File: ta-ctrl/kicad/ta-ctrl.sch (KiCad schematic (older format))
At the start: 24 parts, among them J1 PinSocket_16_ctrl, J2 PinSocket_16_ctrl, J3 MountingHole_ctrl, J4 PinSocket_4_ctrl, J5 PinSocket_4_ctrl, J6 PinSocket_5_ctrl, J7 PinSocket_5_ctrl, U1 LSF0204, U2 LSF0204, U3 LSF0204

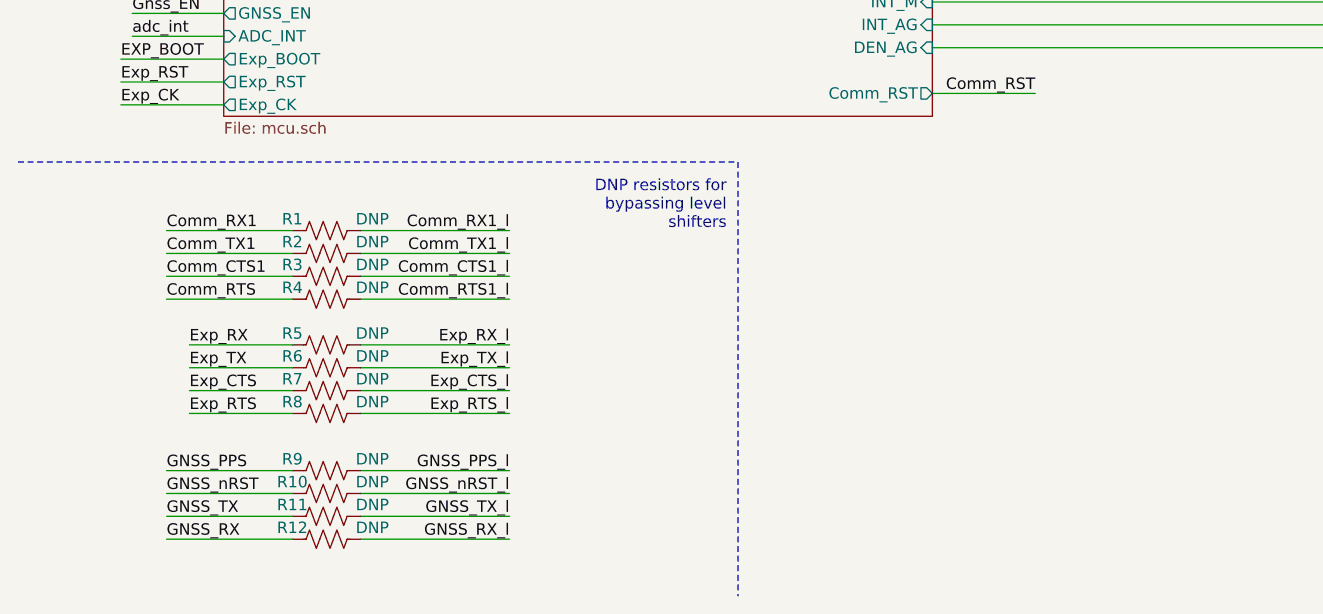
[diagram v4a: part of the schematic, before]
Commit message: updated and checked all footprints, added a diode too
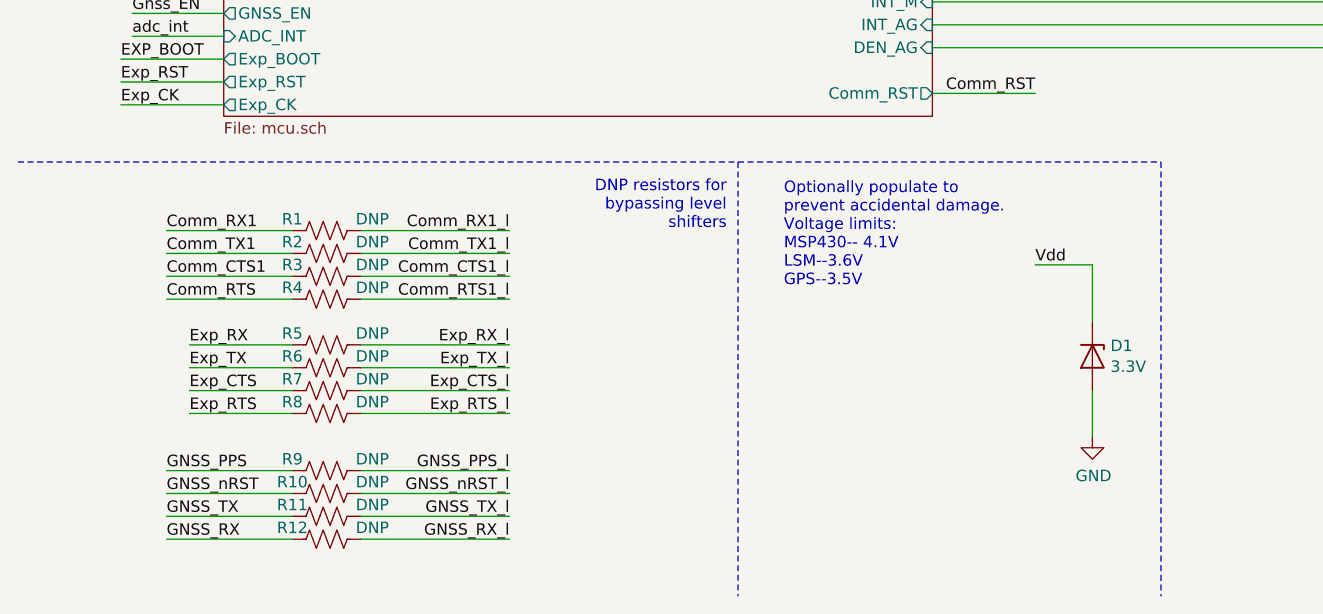
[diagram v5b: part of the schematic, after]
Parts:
- added D1: 3.3V, ta-ctrl:D_SOD-323F, symbol Device:D_Zener
- J1, J2: footprint (none) -> ta-ctrl:PinSocket_1x16_TartanArtibeus_ctrl_cpy
- J3: footprint (none) -> ta-ctrl:MountingHoles_TartanArtibeus_ctrl_cpy
- J4, J5: footprint (none) -> ta-ctrl:PinSocket_1x4_TartanArtibeus_ctrl_cpy
- R1, R10, R11, R12, R13, R14, R2, R3, R4, R5, R6, R7, R8, R9: footprint (none) -> ta-ctrl:R_0603_1608Metric_ctrl_cpy
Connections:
- net GND: now also D1.2 (A)
- net Vdd: now also D1.1 (K)
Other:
- note added: "Optionally populate to\nprevent accidental damage.\nVoltage limits:\nMSP430-- 4.1V\nLSM--3.6V\nGPS--3.5V\n"
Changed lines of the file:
@@
 F 0 "J1" H 1575 1165 50  0000 C CNN
 F 1 "PinSocket_16_ctrl" H 1575 1074 50  0000 C CNN
-F 2 "" H 1150 850 50  0001 C CNN
+F 2 "ta-ctrl:PinSocket_1x16_TartanArtibeus_ctrl_cpy" H 1150 850 50  0001 C CNN
 F 3 "" H 1150 850 50  0001 C CNN
 	1    1550 850
@@
 F 0 "J4" H 3828 963 50  0000 L CNN
 F 1 "PinSocket_4_ctrl" H 3828 872 50  0000 L CNN
-F 2 "" H 3500 850 50  0001 C CNN
+F 2 "ta-ctrl:PinSocket_1x4_TartanArtibeus_ctrl_cpy" H 3500 850 50  0001 C CNN
 F 3 "" H 3500 850 50  0001 C CNN
 	1    3550 850
@@
 F 0 "J5" H 3828 1713 50  0000 L CNN
 F 1 "PinSocket_4_ctrl" H 3828 1622 50  0000 L CNN
-F 2 "" H 3500 1600 50  0001 C CNN
+F 2 "ta-ctrl:PinSocket_1x4_TartanArtibeus_ctrl_cpy" H 3500 1600 50  0001 C CNN
 F 3 "" H 3500 1600 50  0001 C CNN
 	1    3550 1600
@@
 F 0 "J3" H 3728 2563 50  0000 L CNN
 F 1 "MountingHole_ctrl" H 3728 2472 50  0000 L CNN
-F 2 "" H 3300 2450 50  0001 C CNN
+F 2 "ta-ctrl:MountingHoles_TartanArtibeus_ctrl_cpy" H 3300 2450 50  0001 C CNN
 F 3 "" H 3300 2450 50  0001 C CNN
 	1    3450 2450
@@
 F 0 "J2" H 1575 2415 50  0000 C CNN
 F 1 "PinSocket_16_ctrl" H 1575 2324 50  0000 C CNN
-F 2 "" H 1150 2100 50  0001 C CNN
+F 2 "ta-ctrl:PinSocket_1x16_TartanArtibeus_ctrl_cpy" H 1150 2100 50  0001 C CNN
 F 3 "" H 1150 2100 50  0001 C CNN
 	1    1550 2100
@@
 F 1 "LSF0204" H 7050 1734 50  0000 C CNN
 F 2 "ta-ctrl:TSSOP-14" H 6850 1200 50  0001 C CNN
-F 3 "" H 6850 1200 50  0001 C CNN
+F 3 "https://www.ti.com/lit/ds/symlink/lsf0204-q1.pdf?HQS=TI-null-null-digikeymode-df-pf-null-wwe&ts=1595462922658" H 6850 1200 50  0001 C CNN
 	1    7050 1200
 	1    0    0    -1
@@
 F 1 "LSF0204" H 9400 1784 50  0000 C CNN
 F 2 "ta-ctrl:TSSOP-14" H 9200 1250 50  0001 C CNN
-F 3 "" H 9200 1250 50  0001 C CNN
+F 3 "https://www.ti.com/lit/ds/symlink/lsf0204-q1.pdf?HQS=TI-null-null-digikeymode-df-pf-null-wwe&ts=1595462922658" H 9200 1250 50  0001 C CNN
 	1    9400 1250
 	1    0    0    -1
@@
 F 1 "LSF0204" H 8100 3034 50  0000 C CNN
 F 2 "ta-ctrl:TSSOP-14" H 7900 2500 50  0001 C CNN
-F 3 "" H 7900 2500 50  0001 C CNN
+F 3 "https://www.ti.com/lit/ds/symlink/lsf0204-q1.pdf?HQS=TI-null-null-digikeymode-df-pf-null-wwe&ts=1595462922658" H 7900 2500 50  0001 C CNN
 	1    8100 2500
 	1    0    0    -1
 $EndComp
 $Comp
-L power:GND #PWR06
+L power:GND #PWR07
 U 1 1 5F1A8EDE
 P 6550 1600
-F 0 "#PWR06" H 6550 1350 50  0001 C CNN
+F 0 "#PWR07" H 6550 1350 50  0001 C CNN
 F 1 "GND" H 6555 1427 50  0000 C CNN
 F 2 "" H 6550 1600 50  0001 C CNN
@@
 	6550 1400 6550 1600
 $Comp
-L power:GND #PWR07
+L power:GND #PWR08
 U 1 1 5F1B0754
 P 7500 2900
-F 0 "#PWR07" H 7500 2650 50  0001 C CNN
+F 0 "#PWR08" H 7500 2650 50  0001 C CNN
 F 1 "GND" H 7505 2727 50  0000 C CNN
 F 2 "" H 7500 2900 50  0001 C CNN
@@
 	7500 2700 7650 2700
 $Comp
-L power:GND #PWR08
+L power:GND #PWR09
 U 1 1 5F1B8049
 P 8800 1650
-F 0 "#PWR08" H 8800 1400 50  0001 C CNN
+F 0 "#PWR09" H 8800 1400 50  0001 C CNN
 F 1 "GND" H 8805 1477 50  0000 C CNN
 F 2 "" H 8800 1650 50  0001 C CNN
@@
 F 0 "R13" H 9568 2046 50  0000 L CNN
 F 1 "10K" H 9568 1955 50  0000 L CNN
-F 2 "" V 9540 1990 50  0001 C CNN
+F 2 "ta-ctrl:R_0603_1608Metric_ctrl_cpy" V 9540 1990 50  0001 C CNN
 F 3 "~" H 9500 2000 50  0001 C CNN
 	1    9500 2000
@@
 F 0 "R14" H 9918 2046 50  0000 L CNN
 F 1 "10K" H 9918 1955 50  0000 L CNN
-F 2 "" V 9890 1990 50  0001 C CNN
+F 2 "ta-ctrl:R_0603_1608Metric_ctrl_cpy" V 9890 1990 50  0001 C CNN
 F 3 "~" H 9850 2000 50  0001 C CNN
 	1    9850 2000
@@
 F 0 "R3" V 1800 6450 50  0000 C CNN
 F 1 "DNP" V 1800 6800 50  0000 C CNN
-F 2 "" V 1890 6590 50  0001 C CNN
+F 2 "ta-ctrl:R_0603_1608Metric_ctrl_cpy" V 1890 6590 50  0001 C CNN
 F 3 "~" H 1850 6600 50  0001 C CNN
 	1    1850 6600
@@
 F 0 "R2" V 1800 6350 50  0000 C CNN
 F 1 "DNP" V 1800 6700 50  0000 C CNN
-F 2 "" V 1890 6490 50  0001 C CNN
+F 2 "ta-ctrl:R_0603_1608Metric_ctrl_cpy" V 1890 6490 50  0001 C CNN
 F 3 "~" H 1850 6500 50  0001 C CNN
 	1    1850 6500
@@
 F 0 "R1" V 1800 6250 50  0000 C CNN
 F 1 "DNP" V 1800 6600 50  0000 C CNN
-F 2 "" V 1890 6390 50  0001 C CNN
+F 2 "ta-ctrl:R_0603_1608Metric_ctrl_cpy" V 1890 6390 50  0001 C CNN
 F 3 "~" H 1850 6400 50  0001 C CNN
 	1    1850 6400
@@
 F 0 "R4" V 1800 6550 50  0000 C CNN
 F 1 "DNP" V 1800 6900 50  0000 C CNN
-F 2 "" V 1890 6690 50  0001 C CNN
+F 2 "ta-ctrl:R_0603_1608Metric_ctrl_cpy" V 1890 6690 50  0001 C CNN
 F 3 "~" H 1850 6700 50  0001 C CNN
 	1    1850 6700
@@
 F 0 "R7" V 1800 6950 50  0000 C CNN
 F 1 "DNP" V 1800 7300 50  0000 C CNN
-F 2 "" V 1890 7090 50  0001 C CNN
+F 2 "ta-ctrl:R_0603_1608Metric_ctrl_cpy" V 1890 7090 50  0001 C CNN
 F 3 "~" H 1850 7100 50  0001 C CNN
 	1    1850 7100
@@
 F 0 "R6" V 1800 6850 50  0000 C CNN
 F 1 "DNP" V 1800 7200 50  0000 C CNN
-F 2 "" V 1890 6990 50  0001 C CNN
+F 2 "ta-ctrl:R_0603_1608Metric_ctrl_cpy" V 1890 6990 50  0001 C CNN
 F 3 "~" H 1850 7000 50  0001 C CNN
 	1    1850 7000
@@
 F 0 "R5" V 1800 6750 50  0000 C CNN
 F 1 "DNP" V 1800 7100 50  0000 C CNN
-F 2 "" V 1890 6890 50  0001 C CNN
+F 2 "ta-ctrl:R_0603_1608Metric_ctrl_cpy" V 1890 6890 50  0001 C CNN
 F 3 "~" H 1850 6900 50  0001 C CNN
 	1    1850 6900
@@
 F 0 "R8" V 1800 7050 50  0000 C CNN
 F 1 "DNP" V 1800 7400 50  0000 C CNN
-F 2 "" V 1890 7190 50  0001 C CNN
+F 2 "ta-ctrl:R_0603_1608Metric_ctrl_cpy" V 1890 7190 50  0001 C CNN
 F 3 "~" H 1850 7200 50  0001 C CNN
 	1    1850 7200
@@
 F 0 "R11" V 1800 7500 50  0000 C CNN
 F 1 "DNP" V 1800 7850 50  0000 C CNN
-F 2 "" V 1890 7640 50  0001 C CNN
+F 2 "ta-ctrl:R_0603_1608Metric_ctrl_cpy" V 1890 7640 50  0001 C CNN
 F 3 "~" H 1850 7650 50  0001 C CNN
 	1    1850 7650
@@
 F 0 "R10" V 1800 7400 50  0000 C CNN
 F 1 "DNP" V 1800 7750 50  0000 C CNN
-F 2 "" V 1890 7540 50  0001 C CNN
+F 2 "ta-ctrl:R_0603_1608Metric_ctrl_cpy" V 1890 7540 50  0001 C CNN
 F 3 "~" H 1850 7550 50  0001 C CNN
 	1    1850 7550
@@
 F 0 "R9" V 1800 7300 50  0000 C CNN
 F 1 "DNP" V 1800 7650 50  0000 C CNN
-F 2 "" V 1890 7440 50  0001 C CNN
+F 2 "ta-ctrl:R_0603_1608Metric_ctrl_cpy" V 1890 7440 50  0001 C CNN
 F 3 "~" H 1850 7450 50  0001 C CNN
 	1    1850 7450
@@
 F 0 "R12" V 1800 7600 50  0000 C CNN
 F 1 "DNP" V 1800 7950 50  0000 C CNN
-F 2 "" V 1890 7740 50  0001 C CNN
+F 2 "ta-ctrl:R_0603_1608Metric_ctrl_cpy" V 1890 7740 50  0001 C CNN
 F 3 "~" H 1850 7750 50  0001 C CNN
 	1    1850 7750
@@
 Wire Wire Line
 	1150 7750 1700 7750
-Wire Notes Line
-	500  6100 3650 6100
 Wire Notes Line
 	3650 6100 3650 8000
@@
 Wire Wire Line
 	5050 2600 5050 2700
+Text Label 4950 6550 0    50   ~ 0
+Vdd
+Wire Wire Line
+	4950 6550 5200 6550
+Wire Wire Line
+	5200 6550 5200 6800
+$Comp
+L Device:D_Zener D1
+U 1 1 5F1DB801
+P 5200 6950
+F 0 "D1" V 5154 7029 50  0000 L CNN
+F 1 "3.3V" V 5245 7029 50  0000 L CNN
+F 2 "ta-ctrl:D_SOD-323F" H 5200 6950 50  0001 C CNN
+F 3 "https://assets.nexperia.com/documents/data-sheet/BZX84J_SER.pdf" H 5200 6950 50  0001 C CNN
+F 4 "BZX84J-B3V3,115" H 5200 6950 50  0001 C CNN "Manufacturer Part Number"
+F 5 "Digikey" H 5200 6950 50  0001 C CNN "Vendor"
+F 6 "1727-1671-1-ND" H 5200 6950 50  0001 C CNN "Vendor Part Number"
+	1    5200 6950
+	0    1    1    0
+$EndComp
+$Comp
+L power:GND #PWR06
+U 1 1 5F1DC8A8
+P 5200 7300
+F 0 "#PWR06" H 5200 7050 50  0001 C CNN
+F 1 "GND" H 5205 7127 50  0000 C CNN
+F 2 "" H 5200 7300 50  0001 C CNN
+F 3 "" H 5200 7300 50  0001 C CNN
+	1    5200 7300
+	1    0    0    -1
+$EndComp
+Wire Wire Line
+	5200 7100 5200 7300
+Wire Notes Line
+	5500 6100 5500 8000
+Wire Notes Line
+	500  6100 5500 6100
+Text Notes 3850 6650 0    50   ~ 0
+Optionally populate to\nprevent accidental damage.\nVoltage limits:\nMSP430-- 4.1V\nLSM--3.6V\nGPS--3.5V\n
 $EndSCHEMATC

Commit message: all parts placed, about halfway through routing
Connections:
- net Comm_CTS1: now also U1.3 (A2); no longer U1.4 (A3)
- net Comm_CTS1_l: now also U1.12 (B2); no longer U1.11 (B3)
- net Comm_RTS: now also U1.2 (A1); no longer U1.5 (A4)
- net Comm_RTS1_l: now also U1.13 (B1); no longer U1.10 (B4)
- net Comm_RX1: now also U1.4 (A3); no longer U1.2 (A1)
- net Comm_RX1_l: now also U1.11 (B3); no longer U1.13 (B1)
- net Comm_TX1: now also U1.5 (A4); no longer U1.3 (A2)
- net Comm_TX1_l: now also U1.10 (B4); no longer U1.12 (B2)
- net Exp_CTS: now also U2.2 (A1); no longer U2.4 (A3)
- net Exp_CTS_l: now also U2.13 (B1); no longer U2.11 (B3)
- net Exp_RX: now also U2.4 (A3); no longer U2.2 (A1)
- net Exp_RX_l: now also U2.11 (B3); no longer U2.13 (B1)
- net GNSS_PPS: now also U3.5 (A4); no longer U3.2 (A1)
- net GNSS_PPS_l: now also U3.10 (B4); no longer U3.13 (B1)
- net GNSS_RX: now also U3.4 (A3); no longer U3.5 (A4)
- net GNSS_RX_l: now also U3.11 (B3); no longer U3.10 (B4)
- net GNSS_TX: now also U3.3 (A2); no longer U3.4 (A3)
- net GNSS_TX_l: now also U3.12 (B2); no longer U3.11 (B3)
- net GNSS_nRST: now also U3.2 (A1); no longer U3.3 (A2)
- net GNSS_nRST_l: now also U3.13 (B1); no longer U3.12 (B2)
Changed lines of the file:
@@
 F2 "Vdd" I L 6600 4000 50
 F3 "Vdd_GNSS" I L 6600 4150 50
-F4 "SDA" B L 6600 4300 50
-F5 "SCL" B L 6600 4400 50
+F4 "SDA" B L 6600 4950 50
+F5 "SCL" B L 6600 4850 50
 F6 "DRDY_M" B L 6600 5300 50
 F7 "INT_M" B L 6600 5400 50
 F8 "INT_AG" B L 6600 5500 50
 F9 "DEN_AG" B L 6600 5600 50
-F10 "GNSS_TX" O L 6600 4900 50
-F11 "GNSS_RX" I L 6600 5000 50
-F12 "GNSS_PPS" O L 6600 5100 50
-F13 "GNSS_nRST" I L 6600 5200 50
+F10 "GNSS_TX" O L 6600 4700 50
+F11 "GNSS_RX" I L 6600 4600 50
+F12 "GNSS_PPS" O L 6600 4500 50
+F13 "GNSS_nRST" I L 6600 4400 50
 $EndSheet
 NoConn ~ 2850 950
@@
 Wire Wire Line
 	8800 1450 8950 1450
-Text Label 6150 1000 0    50   ~ 0
+Text Label 6150 1200 0    50   ~ 0
 Comm_TX1
+Text Label 6150 1100 0    50   ~ 0
+Comm_RX1
+Text Label 6100 1000 0    50   ~ 0
+Comm_CTS1
 Text Label 6150 900  0    50   ~ 0
-Comm_RX1
-Text Label 6100 1100 0    50   ~ 0
-Comm_CTS1
-Text Label 6150 1200 0    50   ~ 0
 Comm_RTS
 Wire Wire Line
+	6600 900  6150 900
+Wire Wire Line
+	6600 1000 6100 1000
+Wire Wire Line
+	6600 1100 6150 1100
+Wire Wire Line
 	6600 1200 6150 1200
-Wire Wire Line
-	6600 1100 6100 1100
-Wire Wire Line
-	6600 900  6150 900
-Wire Wire Line
-	6600 1000 6150 1000
+Text Label 8050 1100 2    50   ~ 0
+Comm_RX1_l
+Wire Wire Line
+	7500 1100 8050 1100
+Text Label 8050 1200 2    50   ~ 0
+Comm_TX1_l
+Wire Wire Line
+	7500 1200 8050 1200
+Text Label 8050 1000 2    50   ~ 0
+Comm_CTS1_l
 Text Label 8050 900  2    50   ~ 0
-Comm_RX1_l
+Comm_RTS1_l
+Wire Wire Line
+	7500 1000 8050 1000
 Wire Wire Line
 	7500 900  8050 900
-Text Label 8050 1000 2    50   ~ 0
-Comm_TX1_l
-Wire Wire Line
-	7500 1000 8050 1000
-Text Label 8050 1100 2    50   ~ 0
-Comm_CTS1_l
-Text Label 8050 1200 2    50   ~ 0
-Comm_RTS1_l
-Wire Wire Line
-	7500 1100 8050 1100
-Wire Wire Line
-	7500 1200 8050 1200
 Text Label 6250 800  0    50   ~ 0
 COMM
@@
 Wire Wire Line
 	8550 2100 8850 2100
-Text Label 9000 2200 2    50   ~ 0
+Text Label 9000 2400 2    50   ~ 0
 Exp_RX_l
 Text Label 9000 2300 2    50   ~ 0
 Exp_TX_l
 Wire Wire Line
-	8550 2200 9000 2200
+	8550 2400 9000 2400
 Wire Wire Line
 	8550 2300 9000 2300
-Text Label 9000 2400 2    50   ~ 0
+Text Label 9000 2200 2    50   ~ 0
 Exp_CTS_l
 Text Label 9000 2500 2    50   ~ 0
@@
 	8550 2500 9000 2500
 Wire Wire Line
-	8550 2400 9000 2400
+	8550 2200 9000 2200
 Text Label 7300 2500 0    50   ~ 0
 Exp_RTS
-Text Label 7300 2200 0    50   ~ 0
+Text Label 7300 2400 0    50   ~ 0
 Exp_RX
 Text Label 7300 2300 0    50   ~ 0
 Exp_TX
-Text Label 7300 2400 0    50   ~ 0
+Text Label 7300 2200 0    50   ~ 0
 Exp_CTS
 Wire Wire Line
 	7650 2500 7300 2500
 Wire Wire Line
+	7650 2400 7300 2400
+Wire Wire Line
+	7650 2300 7300 2300
+Wire Wire Line
 	7650 2200 7300 2200
-Wire Wire Line
-	7650 2300 7300 2300
-Wire Wire Line
-	7650 2400 7300 2400
 Text Label 7300 2100 0    50   ~ 0
 EXP
@@
 Wire Wire Line
 	8550 2700 9000 2700
+Text Label 10350 1250 2    50   ~ 0
+GNSS_PPS_l
+Wire Wire Line
+	9850 1250 10350 1250
 Text Label 10350 950  2    50   ~ 0
-GNSS_PPS_l
+GNSS_nRST_l
 Wire Wire Line
 	9850 950  10350 950
 Text Label 10350 1050 2    50   ~ 0
-GNSS_nRST_l
+GNSS_TX_l
 Wire Wire Line
 	9850 1050 10350 1050
 Text Label 10350 1150 2    50   ~ 0
-GNSS_TX_l
+GNSS_RX_l
 Wire Wire Line
 	9850 1150 10350 1150
-Text Label 10350 1250 2    50   ~ 0
-GNSS_RX_l
-Wire Wire Line
-	9850 1250 10350 1250
-Text Label 8450 1250 0    50   ~ 0
+Text Label 8450 1150 0    50   ~ 0
 GNSS_RX
-Wire Wire Line
-	8950 1250 8450 1250
-Text Label 8450 1150 0    50   ~ 0
-GNSS_TX
 Wire Wire Line
 	8950 1150 8450 1150
 Text Label 8450 1050 0    50   ~ 0
-GNSS_nRST
+GNSS_TX
 Wire Wire Line
 	8950 1050 8450 1050
 Text Label 8450 950  0    50   ~ 0
+GNSS_nRST
+Wire Wire Line
+	8950 950  8450 950
+Text Label 8450 1250 0    50   ~ 0
 GNSS_PPS
 Wire Wire Line
-	8950 950  8450 950
+	8950 1250 8450 1250
 Text Label 10350 1450 2    50   ~ 0
 Gnss_EN
@@
 Wire Wire Line
 	6350 4150 6600 4150
-Text Label 6350 4300 0    50   ~ 0
+Text Label 6350 4950 0    50   ~ 0
 sda
 Wire Wire Line
-	6350 4300 6600 4300
-Text Label 6350 4400 0    50   ~ 0
+	6350 4950 6600 4950
+Text Label 6350 4850 0    50   ~ 0
 scl
 Wire Wire Line
-	6350 4400 6600 4400
-Text Label 6100 5000 0    50   ~ 0
+	6350 4850 6600 4850
+Text Label 6100 4600 0    50   ~ 0
 GNSS_RX
 Wire Wire Line
-	6600 5000 6100 5000
-Text Label 6100 4900 0    50   ~ 0
+	6600 4600 6100 4600
+Text Label 6100 4700 0    50   ~ 0
 GNSS_TX
 Wire Wire Line
-	6600 4900 6100 4900
+	6600 4700 6100 4700
 Wire Wire Line
 	4500 5800 4950 5800
@@
 Text Label 4950 5100 2    50   ~ 0
 GNSS_PPS_l
-Text Label 6100 5100 0    50   ~ 0
+Text Label 6100 4500 0    50   ~ 0
 GNSS_PPS
-Text Label 6100 5200 0    50   ~ 0
+Text Label 6100 4400 0    50   ~ 0
 GNSS_nRST
 Wire Wire Line
-	6100 5200 6600 5200
-Wire Wire Line
-	6100 5100 6600 5100
-$Sheet
-S 1400 4000 3100 1900
-U 5F1ADB0C
-F0 "MCU" 50
-F1 "mcu.sch" 50
-F2 "Vdd" I L 1400 4100 50
-F3 "TST" I L 1400 4850 50
-F4 "RST" I L 1400 4950 50
-F5 "Comm_RX1" O R 4500 4100 50
-F6 "Comm_TX1" I R 4500 4200 50
-F7 "Exp_RX" O R 4500 4500 50
-F8 "Exp_TX" I R 4500 4600 50
-F9 "Exp_CTS" O R 4500 4700 50
-F10 "Exp_RTS" I R 4500 4800 50
-F11 "GNSS_RX" O R 4500 4900 50
-F12 "GNSS_TX" I R 4500 5000 50
-F13 "SDA" B L 1400 5050 50
-F14 "SCL" B L 1400 5150 50
-F15 "Comm_CTS1" O R 4500 4300 50
-F16 "Comm_RTS1" I R 4500 4400 50
-F17 "Comm_EN" O L 1400 5250 50
-F18 "Exp_EN" O L 1400 5350 50
-F19 "GNSS_EN" O L 1400 5450 50
-F20 "ADC_INT" I L 1400 5550 50
-F21 "DBG1" O L 1400 4350 50
-F22 "DBG2" O L 1400 4450 50
-F23 "DBG0" O L 1400 4250 50
-F24 "Exp_BOOT" O L 1400 5650 50
-F25 "Comm_RST" O R 4500 5800 50
-F26 "Exp_CK" O L 1400 5850 50
-F27 "Exp_RST" O L 1400 5750 50
-F28 "GNSS_nRST" O R 4500 5200 50
-F29 "GNSS_PPS" I R 4500 5100 50
-F30 "DRDY_M" I R 4500 5300 50
-F31 "INT_M" I R 4500 5400 50
-F32 "INT_AG" I R 4500 5500 50
-F33 "DEN_AG" I R 4500 5600 50
-$EndSheet
+	6100 4400 6600 4400
+Wire Wire Line
+	6100 4500 6600 4500
 Wire Wire Line
 	1150 4250 1400 4250
@@
 Wire Wire Line
 	1150 4450 1400 4450
-Wire Wire Line
-	4500 5300 6600 5300
-Wire Wire Line
-	4500 5400 6600 5400
-Wire Wire Line
-	4500 5500 6600 5500
-Wire Wire Line
-	4500 5600 6600 5600
 Text Label 1150 6500 0    50   ~ 0
 Comm_TX1
@@
 Text Notes 3850 6650 0    50   ~ 0
 Optionally populate to\nprevent accidental damage.\nVoltage limits:\nMSP430-- 4.1V\nLSM--3.6V\nGPS--3.5V\n
+Wire Wire Line
+	4500 5300 6600 5300
+Wire Wire Line
+	4500 5400 6600 5400
+$Sheet
+S 1400 4000 3100 1900
+U 5F1ADB0C
+F0 "MCU" 50
+F1 "mcu.sch" 50
+F2 "Vdd" I L 1400 4100 50
+F3 "TST" I L 1400 4850 50
+F4 "RST" I L 1400 4950 50
+F5 "Comm_RX1" O R 4500 4100 50
+F6 "Comm_TX1" I R 4500 4200 50
+F7 "Exp_RX" O R 4500 4500 50
+F8 "Exp_TX" I R 4500 4600 50
+F9 "Exp_CTS" O R 4500 4700 50
+F10 "Exp_RTS" I R 4500 4800 50
+F11 "GNSS_RX" O R 4500 4900 50
+F12 "GNSS_TX" I R 4500 5000 50
+F13 "SDA" B L 1400 5050 50
+F14 "SCL" B L 1400 5150 50
+F15 "Comm_CTS1" O R 4500 4300 50
+F16 "Comm_RTS1" I R 4500 4400 50
+F17 "Comm_EN" O L 1400 5250 50
+F18 "Exp_EN" O L 1400 5350 50
+F19 "GNSS_EN" O L 1400 5450 50
+F20 "ADC_INT" I L 1400 5550 50
+F21 "DBG1" O L 1400 4350 50
+F22 "DBG2" O L 1400 4450 50
+F23 "DBG0" O L 1400 4250 50
+F24 "Exp_BOOT" O L 1400 5650 50
+F25 "Comm_RST" O R 4500 5800 50
+F26 "Exp_CK" O L 1400 5850 50
+F27 "Exp_RST" O L 1400 5750 50
+F28 "GNSS_nRST" O R 4500 5200 50
+F29 "GNSS_PPS" I R 4500 5100 50
+F30 "DRDY_M" I R 4500 5300 50
+F31 "INT_M" I R 4500 5400 50
+F32 "INT_AG" I R 4500 5500 50
+F33 "DEN_AG" I R 4500 5600 50
+$EndSheet
+Wire Wire Line
+	4500 5500 6600 5500
+Wire Wire Line
+	4500 5600 6600 5600
 $EndSCHEMATC
